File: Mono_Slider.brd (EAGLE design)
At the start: 56 x 56 mm, 5 parts

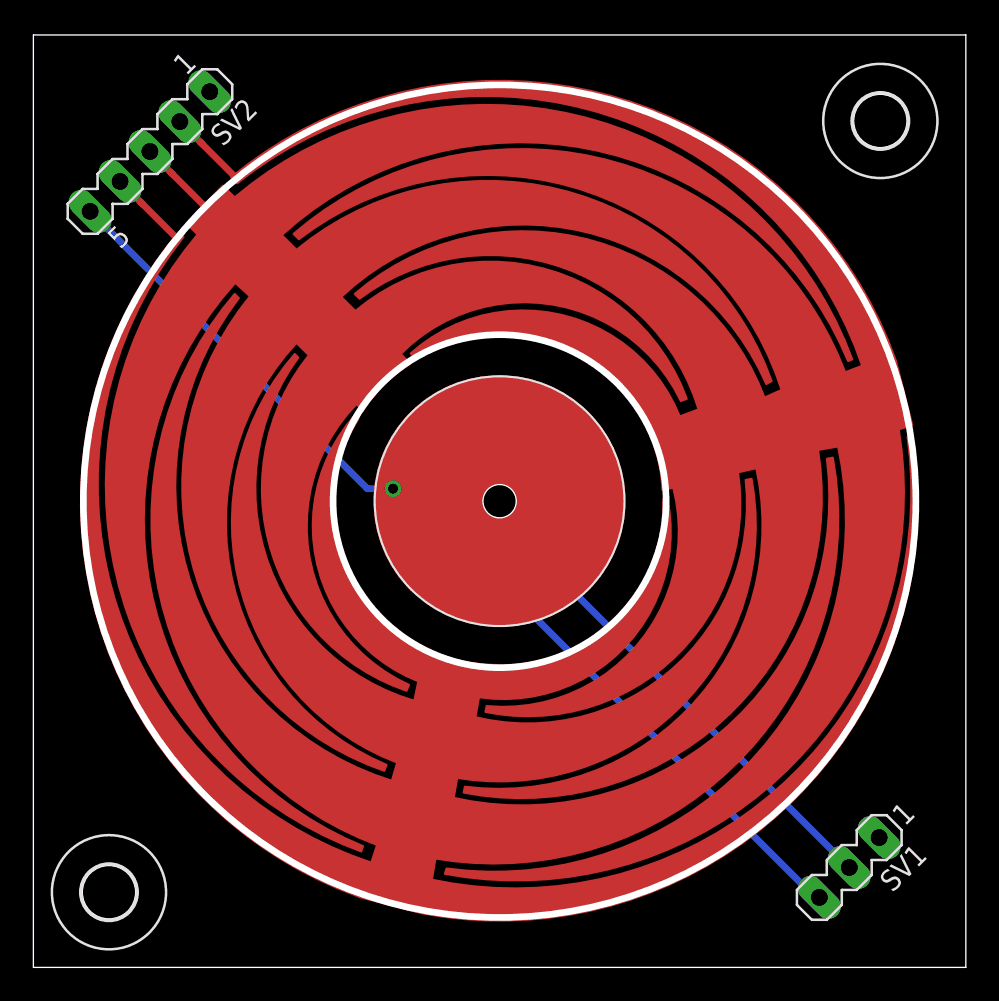
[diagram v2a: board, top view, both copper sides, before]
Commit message: Made round corners and added need gnd pours. TODO Check hatch size, stitching vias, names for pins, version.
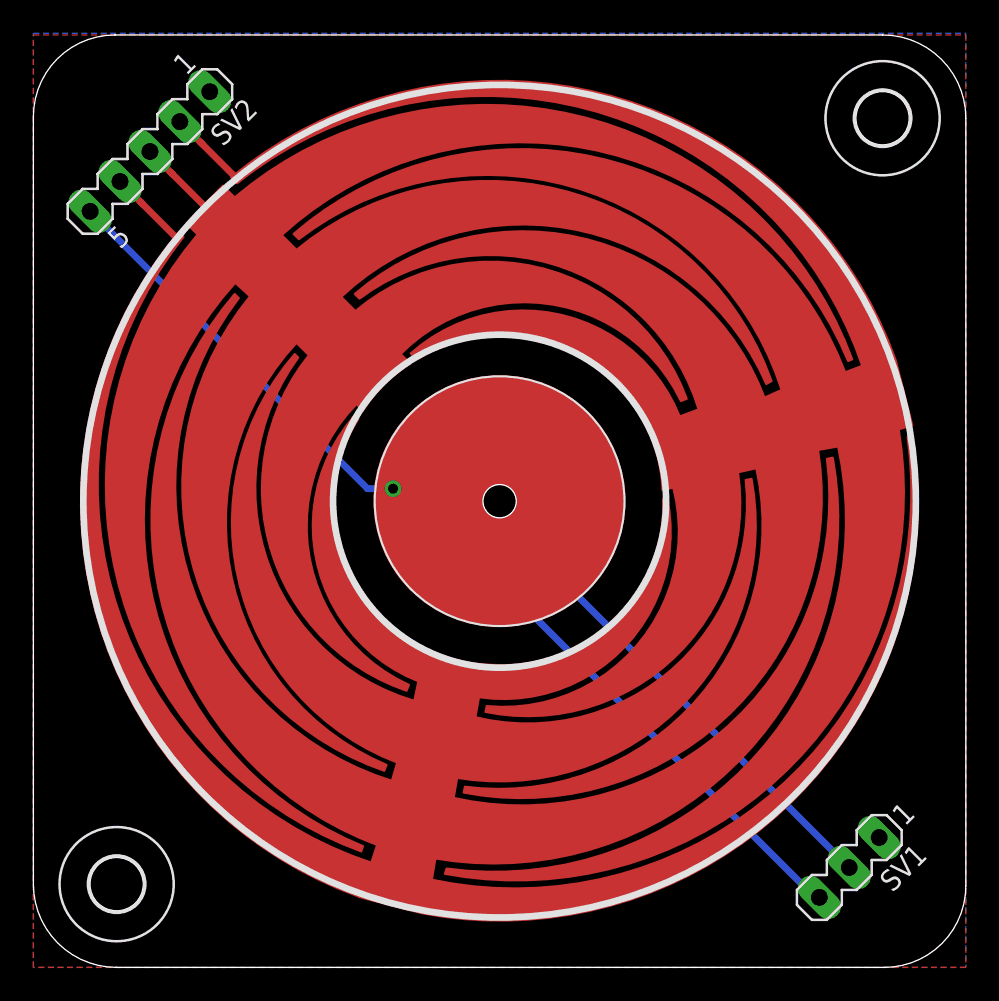
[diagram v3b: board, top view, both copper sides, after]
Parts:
- moved H2 0.67 mm to (5.00, 5.00)
- moved H1 0.21 mm to (51.0, 51.0)
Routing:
- added copper zone on layer 1, net GND
- added copper zone on layer 16, net GND
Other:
- outline, holes or cut-outs redrawn
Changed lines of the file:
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@@
 <setting verticaltext="up"/>
 </settings>
-<grid distance="0.05" unitdist="mm" unit="mm" style="dots" multiple="1" display="yes" altdistance="0.05" altunitdist="mm" altunit="mm"/>
+<grid distance="0.1" unitdist="mm" unit="mm" style="dots" multiple="1" display="yes" altdistance="0.01" altunitdist="mm" altunit="mm"/>
 <layers>
 <layer number="1" name="Top" color="4" fill="1" visible="yes" active="yes"/>
@@
 <layer number="45" name="Holes" color="7" fill="1" visible="yes" active="yes"/>
 <layer number="46" name="Milling" color="3" fill="1" visible="yes" active="yes"/>
-<layer number="47" name="Measures" color="7" fill="1" visible="no" active="yes"/>
+<layer number="47" name="Measures" color="7" fill="1" visible="yes" active="yes"/>
 <layer number="48" name="Document" color="7" fill="1" visible="yes" active="yes"/>
 <layer number="49" name="Reference" color="7" fill="1" visible="yes" active="yes"/>
@@
 <board>
 <plain>
-<wire x1="0" y1="0" x2="56" y2="0" width="0" layer="20"/>
-<wire x1="56" y1="0" x2="56" y2="56" width="0" layer="20"/>
-<wire x1="56" y1="56" x2="0" y2="56" width="0" layer="20"/>
-<wire x1="0" y1="56" x2="0" y2="0" width="0" layer="20"/>
-<dimension x1="0" y1="0" x2="0" y2="80.01" x3="-5.08" y3="40.005" textsize="1.778" layer="47"/>
-<dimension x1="0" y1="80" x2="80.03" y2="80.01" x3="40.01420625" y3="86.355" textsize="1.778" layer="47"/>
+<wire x1="0" y1="5" x2="5" y2="0" width="0.01" layer="20" curve="90"/>
+<wire x1="5" y1="0" x2="51.1" y2="0" width="0.01" layer="20"/>
+<wire x1="51.1" y1="0" x2="56" y2="4.9" width="0.01" layer="20" curve="90"/>
+<wire x1="56" y1="4.9" x2="56" y2="51" width="0.01" layer="20"/>
+<wire x1="56" y1="51" x2="51" y2="56" width="0.01" layer="20" curve="90"/>
+<wire x1="51" y1="56" x2="4.9" y2="56" width="0.01" layer="20"/>
+<wire x1="4.9" y1="56" x2="0" y2="51.1" width="0.01" layer="20" curve="90"/>
+<wire x1="0" y1="51.1" x2="0" y2="5" width="0.01" layer="20"/>
 </plain>
 <attributes>
@@
 <param name="mdViaViaSameLayer" value="8mil"/>
 <param name="mnLayersViaInSmd" value="2"/>
-<param name="mdCopperDimension" value="0.00761875mm"/>
-<param name="mdDrill" value="0.00761875mm"/>
+<param name="mdCopperDimension" value="0.3mm"/>
+<param name="mdDrill" value="0.3mm"/>
 <param name="mdSmdStop" value="0mil"/>
 <param name="msWidth" value="10mil"/>
@@
 </autorouter>
 <elements>
-<element name="H1" library="holes" package="3,2" value="MOUNT-HOLE3.2" x="50.865" y="50.835"/>
-<element name="H2" library="holes" package="3,2" value="MOUNT-HOLE3.2" x="4.54" y="4.515"/>
+<element name="H1" library="holes" package="3,2" value="MOUNT-HOLE3.2" x="51" y="51"/>
+<element name="H2" library="holes" package="3,2" value="MOUNT-HOLE3.2" x="5" y="5"/>
 <element name="SL1" library="SLIDER" package="SLIDER_SMALL" value="SLIDER" x="28" y="28" rot="R45"/>
 <element name="SV1" library="con-lstb" package="MA03-1" value="" x="49" y="6" rot="R225">
@@
 <contactref element="SV1" pad="1"/>
 <contactref element="SV2" pad="1"/>
-<wire x1="50.79605" y1="7.79605" x2="10.5921" y2="52.5921" width="0" layer="19" extent="1-1"/>
+<polygon width="0.3" layer="1" pour="hatch">
+<vertex x="0" y="56"/>
+<vertex x="56" y="56"/>
+<vertex x="56" y="0"/>
+<vertex x="0" y="0"/>
+</polygon>
+<polygon width="0.3" layer="16" pour="hatch">
+<vertex x="0" y="56.1"/>
+<vertex x="56" y="56.1"/>
+<vertex x="56" y="0"/>
+<vertex x="0" y="0"/>
+</polygon>
 </signal>
 <signal name="N$3">

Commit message: Changed hatch, silk and clearence
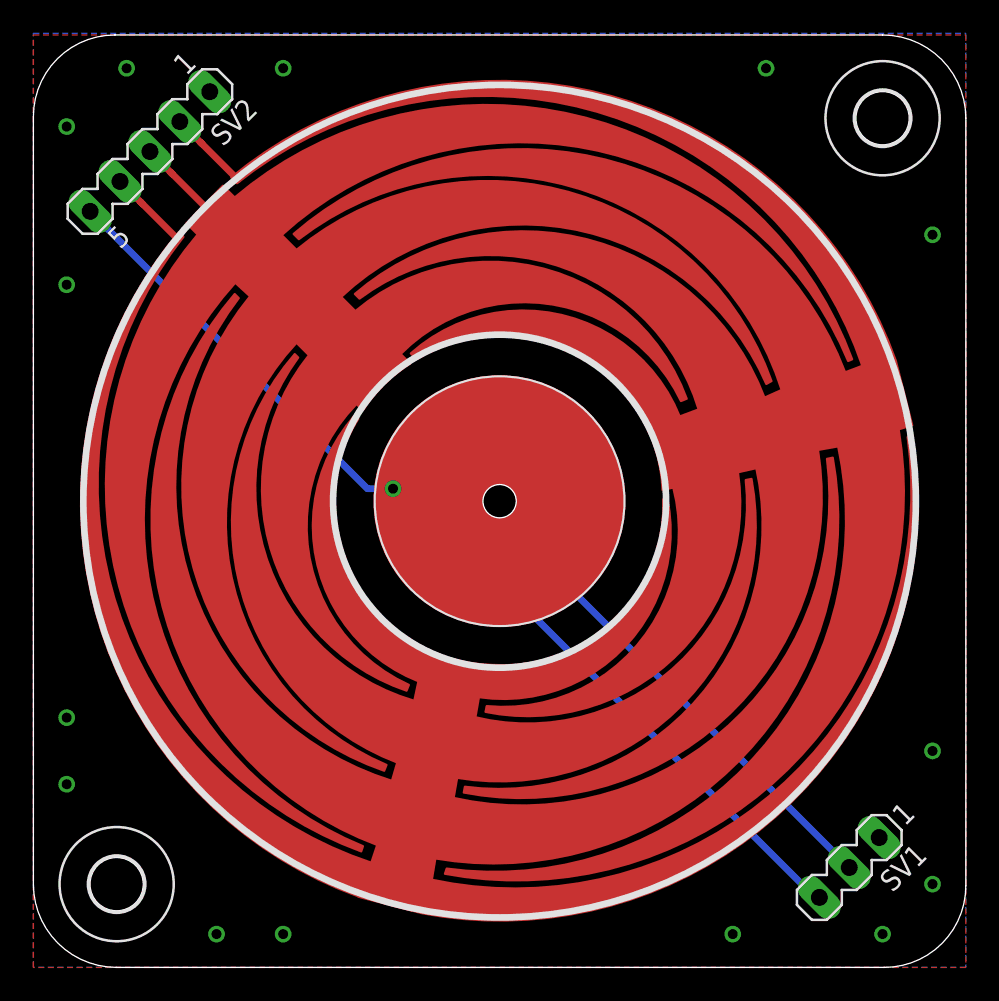
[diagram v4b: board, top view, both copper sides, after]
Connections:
- net N$1 renamed A
- net N$2 renamed K
- net N$3 renamed CP
- net N$4 renamed SP1
- net N$5 renamed SP2
- net N$6 renamed SP3
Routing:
- net CP: track 25.3 -> 27.6 mm
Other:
- board text added: "A"
- board text added: "B"
- board text added: "CP"
- board text added: "GND"
- board text added: "SP1"
- board text added: "SP2"
- board text added: "SP3"
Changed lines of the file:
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@@
 <layer number="23" name="tOrigins" color="15" fill="1" visible="yes" active="yes"/>
 <layer number="24" name="bOrigins" color="15" fill="1" visible="yes" active="yes"/>
-<layer number="25" name="tNames" color="7" fill="1" visible="yes" active="yes"/>
-<layer number="26" name="bNames" color="7" fill="1" visible="yes" active="yes"/>
-<layer number="27" name="tValues" color="7" fill="1" visible="yes" active="yes"/>
-<layer number="28" name="bValues" color="7" fill="1" visible="yes" active="yes"/>
+<layer number="25" name="tNames" color="7" fill="1" visible="no" active="yes"/>
+<layer number="26" name="bNames" color="7" fill="1" visible="no" active="yes"/>
+<layer number="27" name="tValues" color="7" fill="1" visible="no" active="yes"/>
+<layer number="28" name="bValues" color="7" fill="1" visible="no" active="yes"/>
 <layer number="29" name="tStop" color="7" fill="3" visible="yes" active="yes"/>
 <layer number="30" name="bStop" color="7" fill="6" visible="yes" active="yes"/>
@@
 <wire x1="4.9" y1="56" x2="0" y2="51.1" width="0.01" layer="20" curve="90"/>
 <wire x1="0" y1="51.1" x2="0" y2="5" width="0.01" layer="20"/>
+<text x="2.8" y="47" size="1" layer="22" rot="MR0">CP</text>
+<text x="4.6" y="48.7" size="1" layer="22" rot="MR0">SP1</text>
+<text x="6" y="50.5" size="1" layer="22" rot="MR0">SP2</text>
+<text x="7.8" y="52.2" size="1" layer="22" rot="MR0">SP3</text>
+<text x="12.6" y="54.4" size="1" layer="22" rot="MR0">GND</text>
+<text x="49.1" y="2" size="1" layer="22" rot="MR0">A</text>
+<text x="51" y="3.7" size="1" layer="22" rot="MR0">B</text>
+<text x="51.57679375" y="5.513396875" size="1" layer="22" rot="MR120">GND</text>
 </plain>
 <attributes>
@@
 <signal name="N$11">
 </signal>
-<signal name="N$1">
+<signal name="A">
 <contactref element="SL1" pad="A"/>
 <contactref element="SV1" pad="3"/>
@@
 <wire x1="47.45" y1="3.95789375" x2="47.203946875" y2="4.203946875" width="0.4064" layer="16"/>
 </signal>
-<signal name="N$2">
+<signal name="K">
 <contactref element="SL1" pad="K"/>
 <contactref element="SV1" pad="2"/>
@@
 <contactref element="SV1" pad="1"/>
 <contactref element="SV2" pad="1"/>
-<polygon width="0.3" layer="1" pour="hatch">
+<polygon width="0.1778" layer="1" spacing="1.143" pour="hatch">
 <vertex x="0" y="56"/>
 <vertex x="56" y="56"/>
@@
 <vertex x="0" y="0"/>
 </polygon>
-<polygon width="0.3" layer="16" pour="hatch">
+<polygon width="0.1778" layer="16" spacing="1.778" pour="hatch">
 <vertex x="0" y="56.1"/>
 <vertex x="56" y="56.1"/>
@@
 <vertex x="0" y="0"/>
 </polygon>
-</signal>
-<signal name="N$3">
+<via x="44" y="54" extent="1-16" drill="0.6" shape="octagon"/>
+<via x="54" y="44" extent="1-16" drill="0.6" shape="octagon"/>
+<via x="54" y="13" extent="1-16" drill="0.6" shape="octagon"/>
+<via x="54" y="5" extent="1-16" drill="0.6" shape="octagon"/>
+<via x="51" y="2" extent="1-16" drill="0.6" shape="octagon"/>
+<via x="42" y="2" extent="1-16" drill="0.6" shape="octagon"/>
+<via x="15" y="2" extent="1-16" drill="0.6" shape="octagon"/>
+<via x="11" y="2" extent="1-16" drill="0.6" shape="octagon"/>
+<via x="2" y="11" extent="1-16" drill="0.6" shape="octagon"/>
+<via x="2" y="15" extent="1-16" drill="0.6" shape="octagon"/>
+<via x="2" y="41" extent="1-16" drill="0.6" shape="octagon"/>
+<via x="2" y="50.5" extent="1-16" drill="0.6" shape="octagon"/>
+<via x="5.6" y="54" extent="1-16" drill="0.6" shape="octagon"/>
+<via x="15" y="54" extent="1-16" drill="0.6" shape="octagon"/>
+</signal>
+<signal name="CP">
 <contactref element="SL1" pad="CP"/>
 <contactref element="SV2" pad="5"/>
@@
 <wire x1="21.631975" y1="28.718025" x2="21.6" y2="28.75" width="0.4064" layer="1"/>
 <via x="21.6" y="28.75" extent="1-16" drill="0.6" shape="octagon"/>
-<wire x1="21.6" y1="28.75" x2="20.06579375" y2="28.75" width="0.4064" layer="16"/>
+<wire x1="21.6" y1="28.75" x2="20.699996875" y2="28.75" width="0.4064" layer="16"/>
+<wire x1="20.699996875" y1="28.75" x2="20.06579375" y2="28.75" width="0.4064" layer="16"/>
 <wire x1="20.06579375" y1="28.75" x2="3.407896875" y2="45.407896875" width="0.4064" layer="16"/>
-</signal>
-<signal name="N$4">
+<wire x1="20.699996875" y1="28.75" x2="21.499996875" y2="28.46715625" width="0.4064" layer="16"/>
+<wire x1="21.6" y1="28.75" x2="21.499996875" y2="28.46715625" width="0.4064" layer="16"/>
+<wire x1="20.699996875" y1="28.75" x2="21.499996875" y2="29.032840625" width="0.4064" layer="16"/>
+<wire x1="21.6" y1="28.75" x2="21.499996875" y2="29.032840625" width="0.4064" layer="16"/>
+</signal>
+<signal name="SP1">
 <contactref element="SL1" pad="SP1"/>
 <contactref element="SV2" pad="4"/>
@@
 <wire x1="6.567384375" y1="45.840509375" x2="6.447384375" y2="45.960509375" width="0.4064" layer="1"/>
 </signal>
-<signal name="N$5">
+<signal name="SP2">
 <contactref element="SL1" pad="SP2"/>
 <contactref element="SV2" pad="3"/>
@@
 <wire x1="8.363434375" y1="47.636565625" x2="8.243434375" y2="47.7565625" width="0.4064" layer="1"/>
 </signal>
-<signal name="N$6">
+<signal name="SP3">
 <contactref element="SL1" pad="SP3"/>
 <contactref element="SV2" pad="2"/>
